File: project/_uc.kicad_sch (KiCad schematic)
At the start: 35 parts, among them J401 USB_C_Receptacle_USB2.0, SW401 RST, SW402 MOD, U401 esp32-C3FH4X, U402 XL1050, U403 USBLC6-2SC6, Y401 40MHz

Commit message: fixing silk and bom and generating prod/doc files
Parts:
- J401: jlc-part-type (none) -> E; lcsc# (none) -> C22383836
- R401, R402, R403, R404, R405, R407, R408, R409, R411: lcsc# (none) -> C17673
- R406: lcsc# (none) -> C17470
- R410, R412: lcsc# (none) -> C17561
- SW401: jlc-part-type (none) -> E; lcsc# (none) -> C2885193
- SW402: jlc-part-type (none) -> E; lcsc# (none) -> C2885154
- U401: footprint Package_DFN_QFN:QFN-32-1EP_5x5mm_P0.5mm_EP3.6x3.6mm -> Package_DFN_QFN:QFN-32-1EP_5x5mm_P0.5mm_EP3.65x3.65mm; jlc-part-type (none) -> E; lcsc# (none) -> C2858491
- U402: jlc-part-type (none) -> E; lcsc# (none) -> C609746
- U403: jlc-part-type (none) -> E; lcsc# (none) -> C2687116
- Y401: jlc-part-type (none) -> E; lcsc# (none) -> C437132

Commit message: bom fixes
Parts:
- Y401: lcsc# C437132 -> C19191260
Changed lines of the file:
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@@
   (title_block
     (title "WormControl-Relay15x5t15-ControlUI")
-    (date "2024-12-16")
+    (date "2024-12-19")
     (rev "0.1")
     (company "makerspace.lt")
@@
       (effects (font (size 1.27 1.27)) hide)
     )
-    (property "Datasheet" "https://wmsc.lcsc.com/wmsc/upload/file/pdf/v2/lcsc/2304140030_JGHC-O3240000153350_C437132.pdf" (id 3) (at 46.99 104.14 0)
+    (property "Datasheet" "https://wmsc.lcsc.com/wmsc/upload/file/pdf/v2/lcsc/2311101855_SST-SCGYS40X00000YLXWPM_C19191260.pdf" (id 3) (at 46.99 104.14 0)
       (effects (font (size 1.27 1.27)) hide)
     )
@@
       (effects (font (size 1.27 1.27)) hide)
     )
-    (property "lcsc#" "C437132" (id 5) (at 46.99 104.14 0)
-      (effects (font (size 1.27 1.27)) hide)
-    )
+    (property "lcsc#" "C19191260" (id 5) (at 46.99 104.14 0)
+      (effects (font (size 1.27 1.27)) hide)
+    )

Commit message: adjusting hole sizes and adding qfn model
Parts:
- U401: footprint Package_DFN_QFN:QFN-32-1EP_5x5mm_P0.5mm_EP3.65x3.65mm -> -local:QFN-32-1EP_5x5mm_P0.5mm_EP3.65x3.65mm
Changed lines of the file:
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@@
       (effects (font (size 1.27 1.27) bold) (justify left))
     )
-    (property "Footprint" "Package_DFN_QFN:QFN-32-1EP_5x5mm_P0.5mm_EP3.65x3.65mm" (id 2) (at 171.45 68.58 0)
+    (property "Footprint" "-local:QFN-32-1EP_5x5mm_P0.5mm_EP3.65x3.65mm" (id 2) (at 171.45 68.58 0)
       (effects (font (size 1.27 1.27)) hide)
     )

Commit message: few fixes and bumping up version
* reordering id bits
* moving silkscreen around
* adding hole in the center tab
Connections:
- net ID1: now also U401.10 (IO5/ADC2/SPI_MISO); no longer U401.5 (IO1/ADC1_1)
- net ID2: now also U401.9 (IO4/ADC1_4/SPI_SCK); no longer U401.8 (IO3/ADC1_3)
- net ID3: now also U401.8 (IO3/ADC1_3); no longer U401.9 (IO4/ADC1_4/SPI_SCK)
- net ID4: now also U401.5 (IO1/ADC1_1); no longer U401.10 (IO5/ADC2/SPI_MISO)
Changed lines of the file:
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@@
     (effects (font (size 1.27 1.27)) (justify right))
+  )
+  (hierarchical_label "ID3" (shape input) (at 189.23 91.44 0)
+    (effects (font (size 1.27 1.27)) (justify left))
   )
   (hierarchical_label "GND" (shape bidirectional) (at 62.23 146.05 0)
@@
     (effects (font (size 1.27 1.27)) (justify right))
   )
+  (hierarchical_label "ID4" (shape input) (at 189.23 88.9 0)
+    (effects (font (size 1.27 1.27)) (justify left))
+  )
   (hierarchical_label "GND" (shape bidirectional) (at 161.29 121.92 270)
     (effects (font (size 1.27 1.27)) (justify right))
   )
-  (hierarchical_label "DATA" (shape output) (at 189.23 101.6 0)
+  (hierarchical_label "ID2" (shape input) (at 189.23 96.52 0)
     (effects (font (size 1.27 1.27)) (justify left))
   )
-  (hierarchical_label "ID3" (shape input) (at 189.23 96.52 0)
+  (hierarchical_label "DATA" (shape output) (at 189.23 101.6 0)
     (effects (font (size 1.27 1.27)) (justify left))
   )
@@
     (effects (font (size 1.27 1.27)) (justify left))
   )
+  (hierarchical_label "ID1" (shape input) (at 189.23 99.06 0)
+    (effects (font (size 1.27 1.27)) (justify left))
+  )
   (hierarchical_label "CANL" (shape bidirectional) (at 232.41 138.43 0)
     (effects (font (size 1.27 1.27)) (justify left))
@@
   )
   (hierarchical_label "CLOCK" (shape output) (at 189.23 104.14 0)
-    (effects (font (size 1.27 1.27)) (justify left))
-  )
-  (hierarchical_label "ID1" (shape input) (at 189.23 88.9 0)
-    (effects (font (size 1.27 1.27)) (justify left))
-  )
-  (hierarchical_label "ID4" (shape input) (at 189.23 99.06 0)
     (effects (font (size 1.27 1.27)) (justify left))
   )
@@
     (effects (font (size 1.27 1.27)) (justify right))
   )
-  (hierarchical_label "ID2" (shape input) (at 189.23 91.44 0)
-    (effects (font (size 1.27 1.27)) (justify left))
-  )
   (hierarchical_label "SCL" (shape output) (at 116.84 93.98 180)

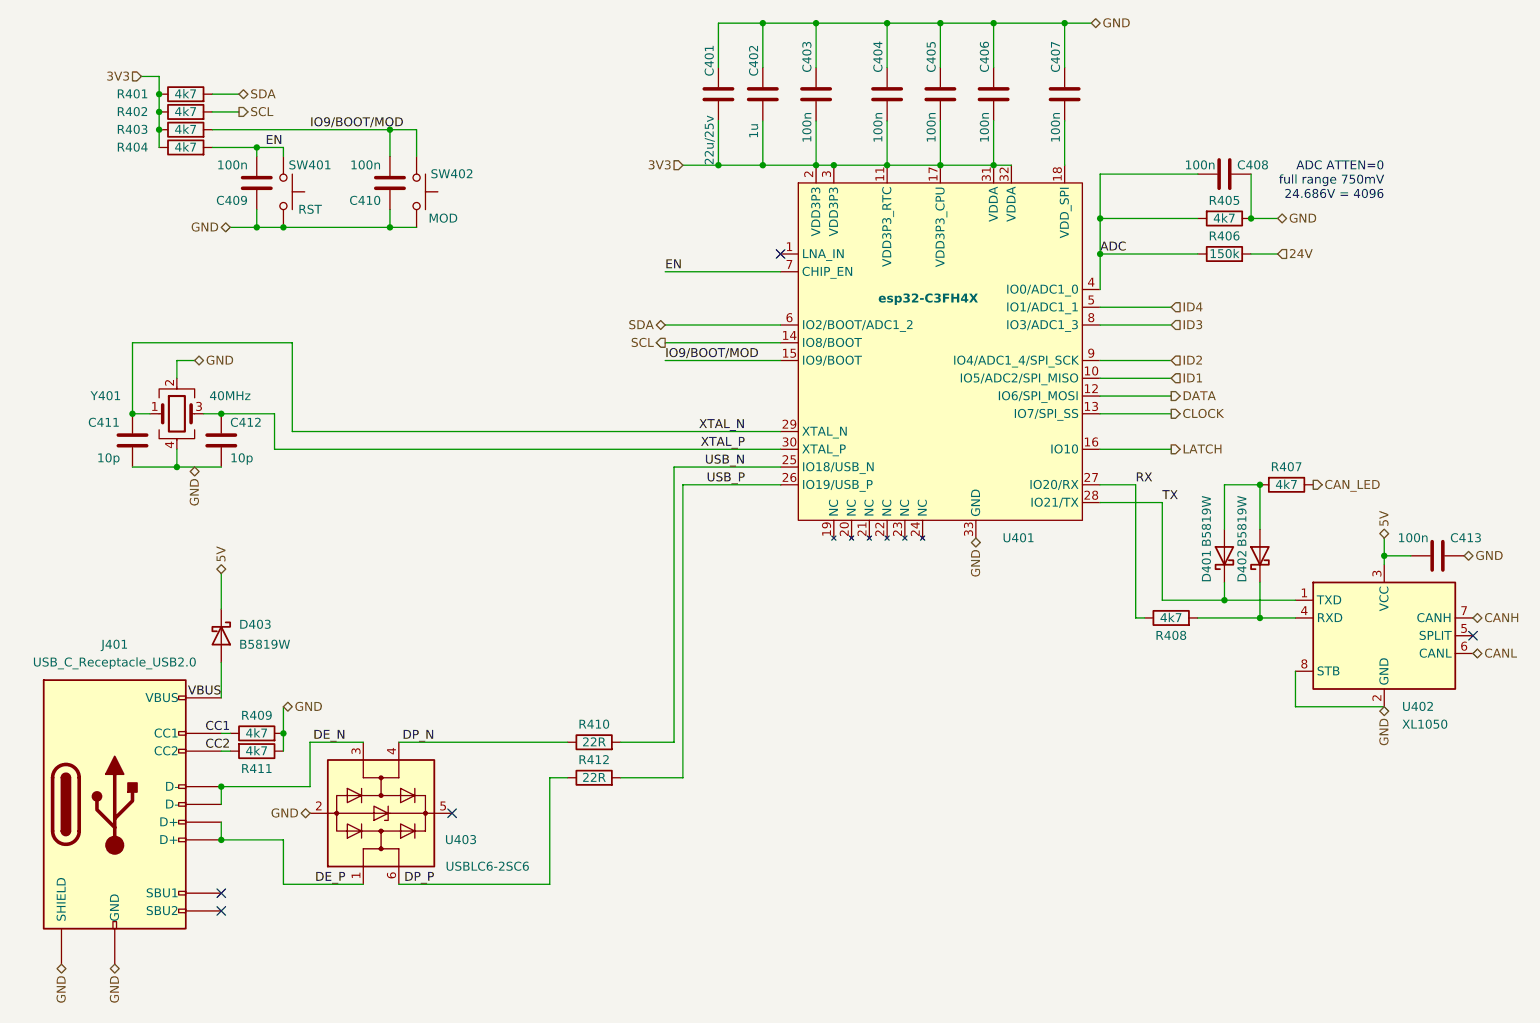
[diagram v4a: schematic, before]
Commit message: improvements for next prototype
* buck makes 6v now
* using LDO for 5v with over voltage disable
* using LDO for 3v3
* adding zener to 24v led to stop it from glowing from 5v USB
* added 0.2mm heigt for USB port hole
* both buttons now 15mm height
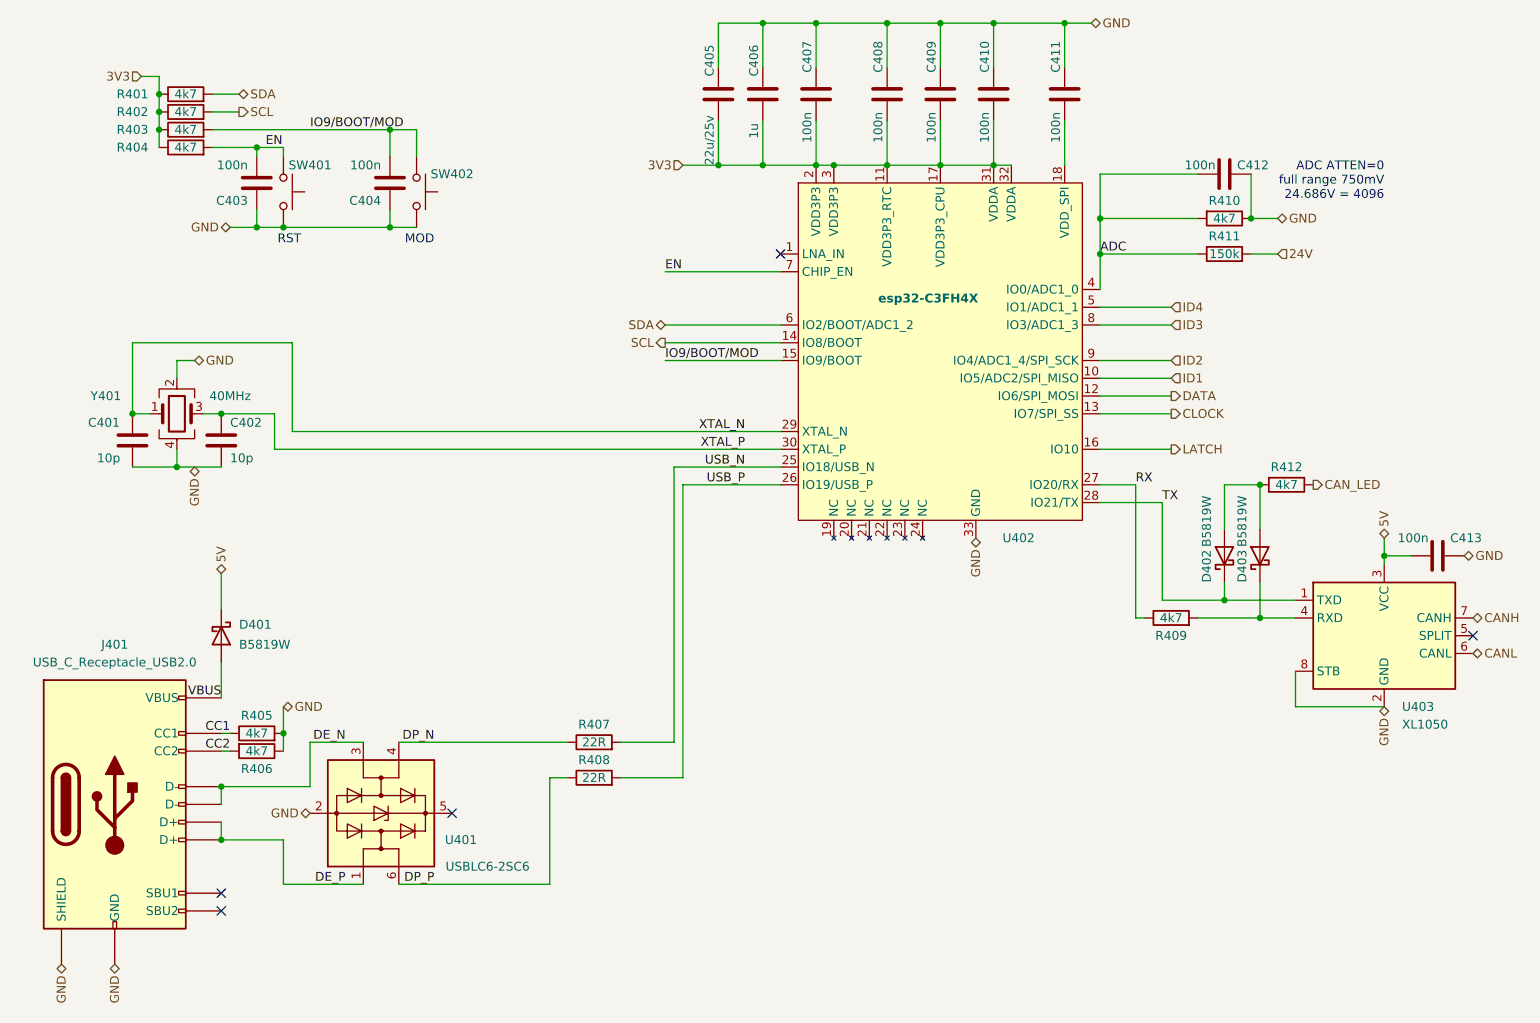
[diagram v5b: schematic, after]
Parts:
- SW401: value RST -> 15mm; footprint -local:SW_SPST_14 -> -local:SW_SPST_15; lcsc# C2885193 -> C2885154
- SW402: value MOD -> 15mm
- renumbered C411 to C401, C412 to C402, C409 to C403, C410 to C404, C401 to C405, C402 to C406, C403 to C407, C404 to C408, C405 to C409, C406 to C410, C407 to C411, C408 to C412, D403 to D401, D401 to D402, D402 to D403, R409 to R405, R411 to R406, R410 to R407, R412 to R408, R408 to R409, R405 to R410, R406 to R411, R407 to R412, U403 to U401, U401 to U402, U402 to U403
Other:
- note added: "MOD"
- note added: "RST"
